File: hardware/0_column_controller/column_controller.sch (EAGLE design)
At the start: 47 parts, among them J3 RJ45, J4 JTAG, J5 JTAG, J7 RJ45, U1 PCA9615

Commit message: remove 5V from AREF pin
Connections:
- net 5V: no longer U$13.AREF
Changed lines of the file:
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@@
 <wire x1="210.82" y1="167.64" x2="210.82" y2="177.8" width="0.1524" layer="91"/>
 <pinref part="SUPPLY5" gate="G$1" pin="5V"/>
-<pinref part="U$13" gate="G$1" pin="AREF"/>
-<wire x1="203.2" y1="165.1" x2="210.82" y2="165.1" width="0.1524" layer="91"/>
-<wire x1="210.82" y1="165.1" x2="210.82" y2="167.64" width="0.1524" layer="91"/>
-<junction x="210.82" y="167.64"/>
 </segment>
 <segment>

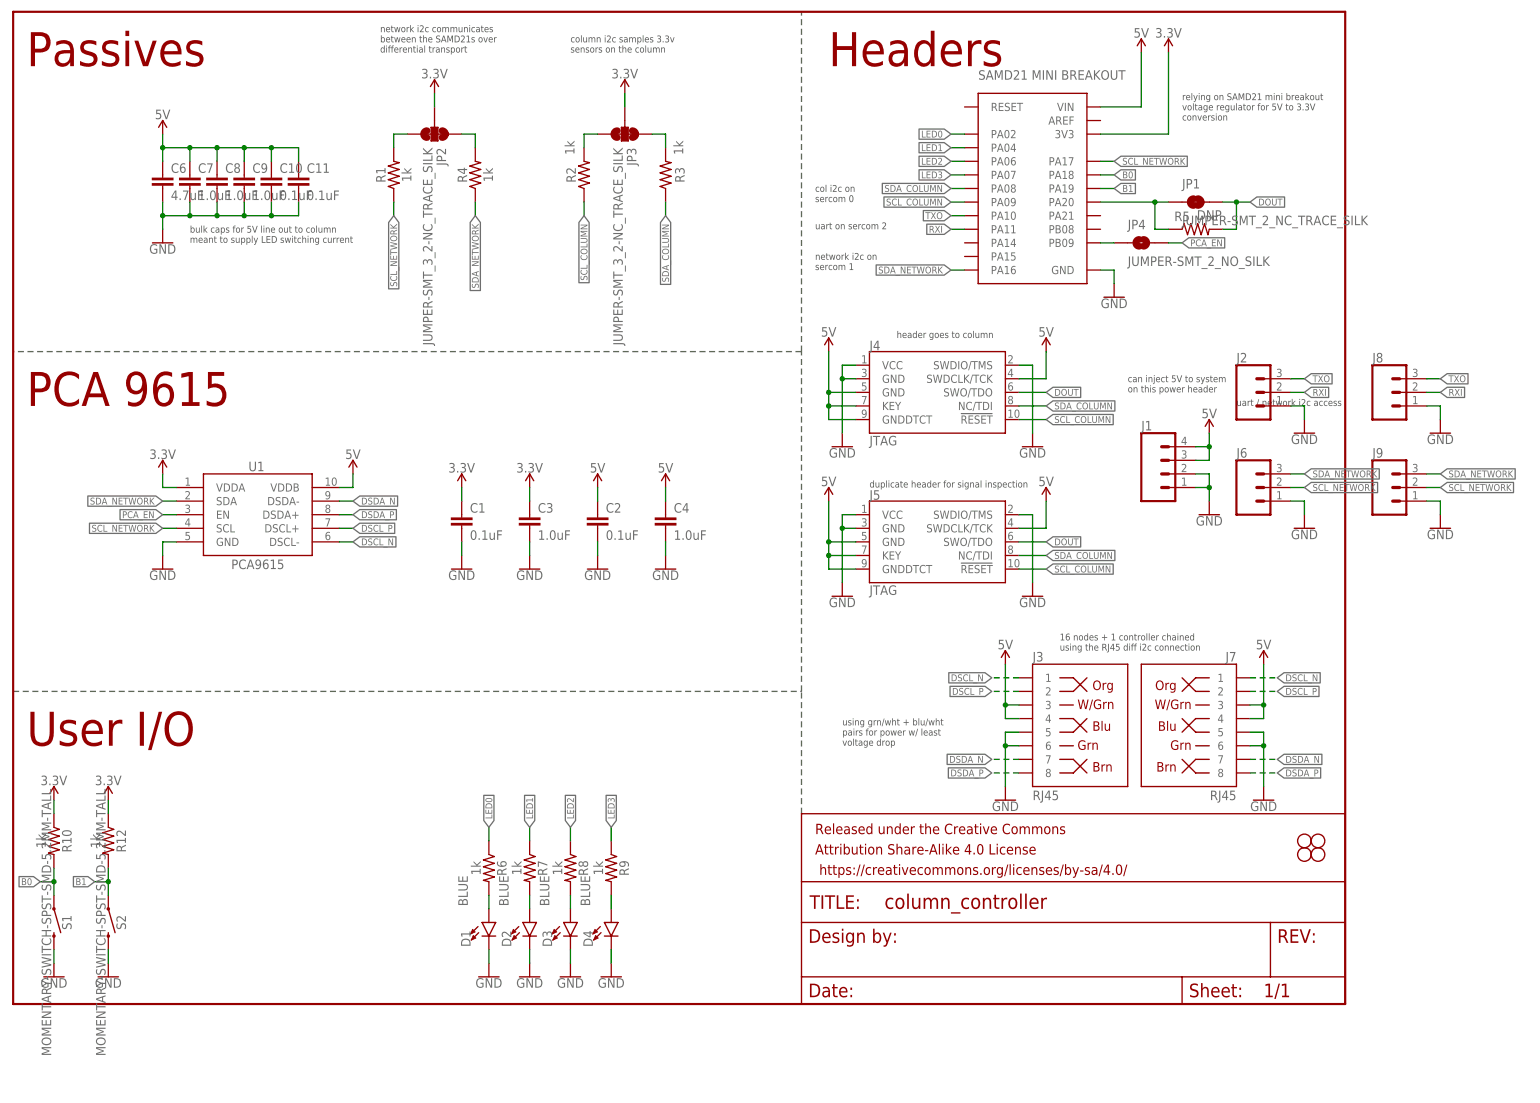
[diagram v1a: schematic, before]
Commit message: change column controller back to esp32 w/ more leds
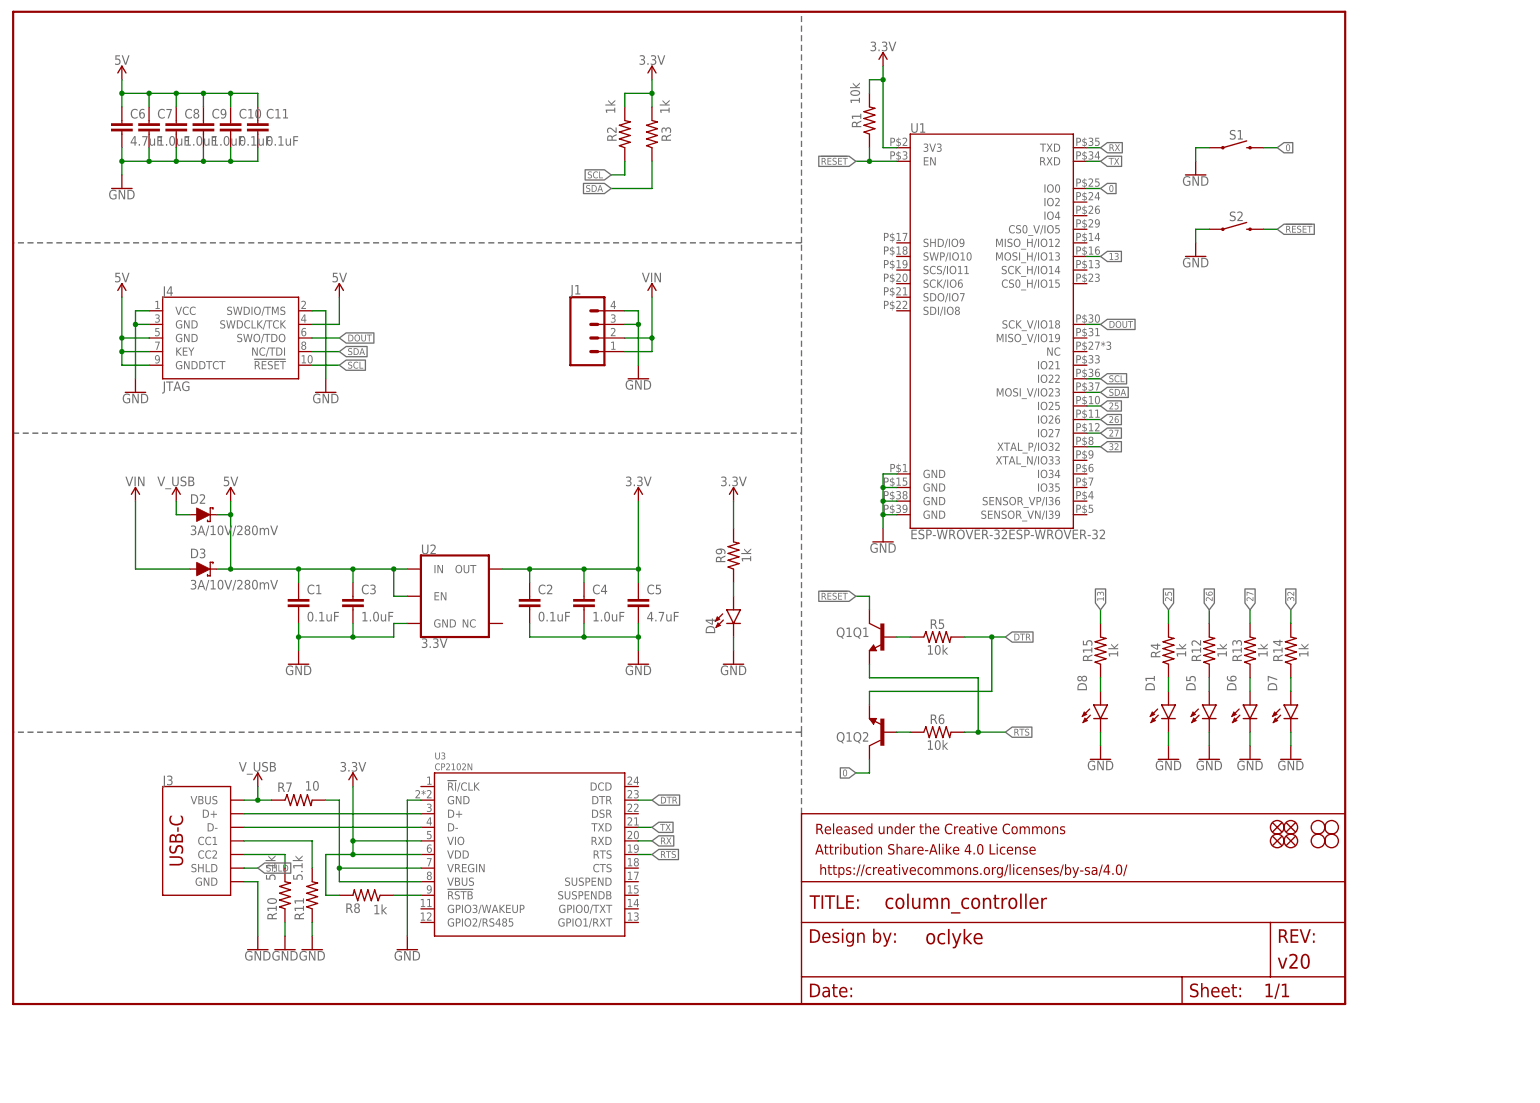
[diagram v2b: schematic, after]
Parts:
- removed J2, J6, J8, J9: (no value), SparkFun-Connectors:CONN_031X03_NO_SILK
- removed J5: JTAG, SparkFun-Connectors:CORTEX_JTAG_DEBUG_SMD
- removed J7: RJ45, SparkFun-Connectors:RJ45-8
- removed JP1: JUMPER-SMT_2_NC_TRACE_SILK, SparkFun-Jumpers:JUMPER-SMT_2_NC_TRACE_SILK
- removed JP2, JP3: JUMPER-SMT_3_2-NC_TRACE_SILK, SparkFun-Jumpers:JUMPER-SMT_3_2-NC_TRACE_SILK
- removed JP4: JUMPER-SMT_2_NO_SILK, SparkFun-Jumpers:JUMPER-SMT_2_NO_SILK
- removed U$13: SAMD21_MINI_BREAKOUT, SparkFun-Boards:SAMD21_MINI_BREAKOUT
- added C5: 4.7uF, SparkFun-Capacitors:4.7UF-0603-35V-(20%)
- added D5, D6, D7, D8: (no value), SparkFun-LED:LED-BLUE0603
- added FD1, FD2, FD3, FD4: FIDUCIAL1X2, SparkFun-Aesthetics:FIDUCIAL1X2
- added Q1: (no value), SparkFun-DiscreteSemi:TRANS_NPN_DUAL-MBT3904DW1T1
- added R11: 5.1k, SparkFun-Resistors:5.1KOHM5.1KOHM-0603-1/10W-1%
- added R13, R14, R15: 1k, SparkFun-Resistors:1KOHM-0603-1/10W-1%
- added U2: 3.3V, SparkFun-IC-Power:V_REG_AP2112K-3.3V
- added U3: CP2102N, SparkFun-IC-Comms:CP2102N
- C6: device SparkFun-Capacitors:4.7UF-0603-6.3V-(10%) -> SparkFun-Capacitors:4.7UF-0603-35V-(20%)
- D1: value BLUE -> (none)
- D2, D3: value BLUE -> 3A/10V/280mV; device SparkFun-LED:LED-BLUE0603 -> SparkFun-DiscreteSemi:DIODE-SCHOTTKY-BAT60A
- D4: value BLUE -> (none); device SparkFun-LED:LED-BLUE0603 -> SparkFun-LED:LED-RED0603
- FRAME1: DESIGNER (none) -> oclyke; REV (none) -> v20
- J1: device SparkFun-Connectors:CONN_04SCREW_LOCK -> SparkFun-Connectors:CONN_04SCREW
- J3: value RJ45 -> (none); device SparkFun-Connectors:RJ45-8 -> SparkFun-Connectors:USB_C_2-LAYER
- R1, R6: value 1k -> 10k; device SparkFun-Resistors:1KOHM-0603-1/10W-1% -> SparkFun-Resistors:10KOHM-0603-1/10W-1%
- R10: value 1k -> 5.1k; device SparkFun-Resistors:1KOHM-0603-1/10W-1% -> SparkFun-Resistors:5.1KOHM5.1KOHM-0603-1/10W-1%
- R5: value DNP -> 10k; device SparkFun-Resistors:RESISTOR0603 -> SparkFun-Resistors:10KOHM-0603-1/10W-1%
- R7: value 1k -> 10; device SparkFun-Resistors:1KOHM-0603-1/10W-1% -> SparkFun-Resistors:10OHM-0603-1/10W-1%
- S1, S2: value MOMENTARY-SWITCH-SPST-SMD-5.2MM-TALL -> MOMENTARY-SWITCH-SPST-SMD-4.6X2.8MM; device SparkFun-Switches:MOMENTARY-SWITCH-SPST-SMD-5.2MM-TALL -> SparkFun-Switches:MOMENTARY-SWITCH-SPST-SMD-4.6X2.8MM
- U1: value PCA9615 -> ESP-WROVER-32ESP-WROVER-32; device SparkFun-IC-Comms:PCA9615 -> SparkFun-RF:ESP-WROVER-32ESP-WROVER-32
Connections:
- removed net B0: R10.2, S1.1, U$13.PA18
- removed net B1: R12.2, S2.1, U$13.PA19
- removed net DSCL_N: J3.1, J7.1, U1.DSCL-
- removed net DSCL_P: J3.2, J7.2, U1.DSCL+
- removed net DSDA_N: J3.7, J7.7, U1.DSDA-
- removed net DSDA_P: J3.8, J7.8, U1.DSDA+
- removed net LED0: R6.1, U$13.PA02
- removed net LED1: R7.1, U$13.PA04
- removed net LED2: R8.1, U$13.PA06
- removed net LED3: R9.1, U$13.PA07
- removed net PCA_EN: JP4.2, U1.EN
- removed net RXI: J2.2, J8.2, U$13.PA11
- removed net SCL_COLUMN: J4.!RESET, J5.!RESET, R2.1, U$13.PA09
- removed net SCL_NETWORK: J6.2, J9.2, R1.1, U$13.PA17, U1.SCL
- removed net SDA_COLUMN: J4.NC/TDI, J5.NC/TDI, R3.1, U$13.PA08
- removed net SDA_NETWORK: J6.3, J9.3, R4.1, U$13.PA16, U1.SDA
- removed net TXO: J2.3, J8.3, U$13.PA10
- new net !RESET: Q1Q1.C, R1.1, S2.2, U1.EN
- new net 0: Q1Q2.C, S1.2, U1.IO0
- new net 13: R15.2, U1.MOSI_H/IO13
- new net 25: R4.2, U1.IO25
- new net 26: R12.2, U1.IO26
- new net 27: R13.2, U1.IO27
- new net 32: R14.2, U1.XTAL_P/IO32
- new net DTR: Q1Q2.E, R5.2, U3.DTR
- new net N$11: J3.CC2, R10.2
- new net N$12: D6.A, R13.1
- new net N$13: D7.A, R14.1
- new net N$14: D8.A, R15.1
- new net RTS: Q1Q1.E, R6.2, U3.RTS
- new net RX: U1.TXD, U3.RXD
- new net SCL: J4.!RESET, R2.1, U1.IO22
- new net SDA: J4.NC/TDI, R3.1, U1.MOSI_V/IO23
- new net SHLD: J3.SHLD
- new net TX: U1.RXD, U3.TXD
- new net VIN: D3.A, J1.1, J1.2
- new net V_USB: D2.A, J3.VBUS, R7.1
- net 3.3V: now also C2.1, C4.1, C5.1, R1.2, R2.2, R3.2, R8.2, R9.2, U1.3V3, U2.OUT, U3.VDD, U3.VIO; no longer C1.1, C3.1, JP2.2, JP3.2, R10.1, R12.1, U$13.3V3, U1.VDDA
- net 5V: now also C1.1, C3.1, D2.C, D3.C, U2.EN, U2.IN; no longer C2.1, C4.1, J1.3, J1.4, J3.3, J3.4, J5.GND@5, J5.GNDDTCT, J5.KEY, J5.SWDCLK/TCK, J7.3, J7.4, U$13.VIN, U1.VDDB
- net DOUT: now also U1.SCK_V/IO18; no longer J5.SWO/TDO, JP1.2, R5.2
- net GND: now also C5.2, D5.C, D6.C, D7.C, D8.C, J1.3, J1.4, J3.GND, R10.1, R11.1, S1.1, S2.1, U1.GND@1, U1.GND@15, U1.GND@38, U2.GND, U3.GND; no longer D2.C, D3.C, J1.1, J1.2, J2.1, J3.5, J3.6, J5.GND@3, J5.SWDIO/TMS, J5.VCC, J6.1, J7.5, J7.6, J8.1, J9.1, S1.2, S2.2, U$13.GND
- net N$1: now also J3.D-, U3.D-; no longer JP1.1, R5.1, U$13.PA20
- net N$10: now also J3.CC1, R11.2; no longer JP4.1, U$13.PB09
- net N$2: now also J3.D+, U3.D+; no longer JP2.3, R1.2
- net N$3: now also Q1Q2.B, R6.1; no longer JP2.1, R4.2
- net N$4: now also D1.A, R4.1; no longer JP3.3, R2.2
- net N$5: now also Q1Q1.B, R5.1; no longer JP3.1, R3.2
- net N$6: now also R7.2, U3.VBUS, U3.VREGIN; no longer D1.A, R6.2
- net N$7: now also R8.1, U3.!RSTB; no longer D4.A, R9.2
- net N$8: now also D4.A, R9.1; no longer D3.A, R8.2
- net N$9: now also D5.A, R12.1; no longer D2.A, R7.2
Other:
- note removed: "16 nodes + 1 controller chained using the RJ45 diff i2c connection"
- note removed: "Headers"
- note removed: "PCA 9615"
- note removed: "Passives"
- note removed: "User I/O"
- note removed: "bulk caps for 5V line out to column meant to supply LED switching current"
- note removed: "can inject 5V to system on this power header"
- note removed: "col i2c on sercom 0"
- note removed: "column i2c samples 3.3v sensors on the column"
- note removed: "duplicate header for signal inspection"
- note removed: "header goes to column"
- note removed: "network i2c communicates between the SAMD21s over differential transport"
- note removed: "network i2c on sercom 1"
- note removed: "relying on SAMD21 mini breakout voltage regulator for 5V to 3.3V conversion"
- note removed: "uart / network i2c access"
- note removed: "uart on sercom 2"
- note removed: "using grn/wht + blu/wht pairs for power w/ least voltage drop"
- moved on the sheet: C1, C10, C11, C2, C3, C4, C6, C7, C8, C9, D1, D4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
